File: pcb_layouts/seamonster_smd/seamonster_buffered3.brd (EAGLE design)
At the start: 172.5 x 106.5 mm, 132 parts, among them IC1 7808DT, IC2 4051D, IC3 4051D, IC4 DG408DY, IC5 4046D, IC6 40106D, IC7 4070D, IC8 4046D, IC9 4040D, Q1 THONKICONNNEW, Q2 THONKICONNNEW, Q3 THONKICONNNEW, Q4 THONKICONNNEW, Q5 THONKICONNNEW, Q6 THONKICONNNEW, SW1 SPDT ON-ON, SW2 SPDT ON-ON, SW3 SPDT ON-ON, SW4 SPDT ON-ON, U1 TL084, U2 TL084, U3 TL084

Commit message: finished routing, working on silkscreen
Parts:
- removed C30, C31, C32, C33, C34, C35: (no value), SparkFun-Capacitors:0805
- added C36, C37, C38, C39, C40, C41: (no value), SparkFun-Capacitors:CPOL-RADIAL-10UF-25V
- added CVCO1, CVCO2: 1µF, SparkFun-Capacitors:0805
- added U4: TL084D, linear:SO14
- C23, C24: value 1µF -> 0.1µF
- IC2: value 4051D -> 40106D; device 40xx:SO16 -> 40xx:SO14
- IC3: value 4051D -> 4040D
- IC4: value DG408DY -> 4051D; device maxim:SO16 -> 40xx:SO16
- IC5: value 4046D -> 4051D
- IC6: value 40106D -> DG408DY; device 40xx:SO14 -> maxim:SO16
- IC7: value 4070D -> 4046D; device 40xx:SO14 -> 40xx:SO16
- IC9: value 4040D -> 4070D; device 40xx:SO16 -> 40xx:SO14
- R1, R10, R11, R12, R13, R14, R2, R3, R4, R5, R6, R7, R8, R9: value (none) -> 270Ω
- moved IC3 126.9 mm to (133.3, 38.1), turned to 0 degrees
- moved IC9 118.1 mm to (21.3, 75.2), flipped to the bottom, turned to 180 degrees
- moved IC7 100.3 mm to (118.6, 51.0), flipped to the top, turned to 0 degrees
- moved IC4 89.2 mm to (19.7, 94.6), turned to 90 degrees
- moved IC5 74.8 mm to (57.8, 94.6), turned to 90 degrees
- moved IC6 66.3 mm to (105.4, 69.8), flipped to the top, turned to 270 degrees
- moved IC2 26.5 mm to (39.4, 75.6), flipped to the bottom, turned to 180 degrees
- moved C23 14.6 mm to (112.3, 32.5), turned to 270 degrees
- moved C24 6.80 mm to (111.3, 39.6), turned to 180 degrees
- moved C17 2.03 mm to (33.0, 75.1), flipped to the top
- moved C5 2.00 mm to (47.0, 56.0)
- moved U$2 1.14 mm to (161.5, 64.3)
- moved C1 1.02 mm to (108.2, 33.0)
- moved C20 0.71 mm to (14.8, 72.8)
- moved C27 0.51 mm to (125.6, 38.1)
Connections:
- removed net N$73: CCO1.P$3_SLEEVE, CCO2.P$3_SLEEVE, CCO3.P$3_SLEEVE, CCO4.P$3_SLEEVE, COMPLEX1.P$3_SLEEVE, COMPLEX2.P$3_SLEEVE
- removed net Q1: IC9.9, J1.2, Q1.P$1_TIP, R9.1
- new net N$61: IC3.9, U3.10
- new net Q1BUFFERED: J1.2, Q1.P$1_TIP, R9.1, U3.8, U3.9
- new net Q2BUFFERED: J2.2, Q2.P$1_TIP, R10.1, U3.13, U3.14
- new net Q3BUFFERED: J3.2, Q3.P$1_TIP, R11.1, U4.1, U4.2
- new net Q4BUFFERED: Q4.P$1_TIP, R12.1, U4.6, U4.7
- new net Q5BUFFERED: Q5.P$1_TIP, R13.1, U4.8, U4.9
- new net Q6BUFFERED: Q6.P$1_TIP, R14.1, U4.13, U4.14
- net A: now also IC4.11, IC5.11, IC6.1; no longer IC2.11, IC3.11, IC4.1
- net B: now also IC4.10, IC5.10, IC6.16; no longer IC2.10, IC3.10, IC4.16
- net C: now also IC4.9, IC5.9, IC6.15; no longer IC2.9, IC3.9, IC4.15
- net CCO1_BUFFERED: now also IC9.2; no longer IC7.2
- net CCO2_BUFFERED: now also IC9.6; no longer IC7.6
- net CCO3_BUFFERED: now also IC9.9; no longer IC7.9
- net CCO4_BUFFERED: now also IC9.13; no longer IC7.13
- net CV_OUT: now also IC4.3; no longer IC3.3
- net CV_OUT_BUFFERED: now also IC7.9; no longer IC5.9
- net GND: now also C23.2, C24.2, C36.2, C37.2, C38.2, C39.2, C40.2, C41.2, CCO1.P$3_SLEEVE, CCO2.P$3_SLEEVE, CCO3.P$3_SLEEVE, CCO4.P$3_SLEEVE, COMPLEX1.P$3_SLEEVE, COMPLEX2.P$3_SLEEVE, IC3.11, IC4.6, IC4.7, IC4.8, IC5.6, IC5.7, IC6.14, IC7.5, IC7.8, IC9.7; no longer C30.2, C31.2, C32.2, C33.2, C34.2, C35.2, IC2.6, IC2.8, IC3.6, IC3.7, IC4.14, IC5.5, IC6.7, IC7.7, IC9.11, IC9.8
- net INV_B_IN: now also IC2.3; no longer IC6.3
- net INV_B_OUT: now also IC2.4; no longer IC6.4
- net INV_C_IN: now also IC2.5; no longer IC6.5
- net INV_C_OUT: now also IC2.6; no longer IC6.6
- net INV_D_IN: now also IC2.9; no longer IC6.9
- net INV_D_OUT: now also IC2.8; no longer IC6.8
- net INV_E_IN: now also IC2.11; no longer IC6.11
- net INV_E_OUT: now also IC2.10; no longer IC6.10
- net MUX1: now also IC6.4; no longer IC4.4
- net MUX2: now also IC6.5; no longer IC4.5
- net MUX3: now also IC6.6; no longer IC4.6
- net MUX4: now also IC6.7; no longer IC4.7
- net MUX5: now also IC6.12; no longer IC4.12
- net MUX6: now also IC6.11; no longer IC4.11
- net MUX7: now also IC6.10; no longer IC4.10
- net MUX8: now also IC6.9; no longer IC4.9
- net N$1: now also IC6.8; no longer IC4.8
- net N$18: now also IC4.13; no longer IC3.13
- net N$19: now also IC5.13; no longer IC2.13
- net N$2: now also IC2.1; no longer IC6.1
- net N$20: now also IC5.14; no longer IC2.14
- net N$21: now also IC5.15; no longer IC2.15
- net N$22: now also IC5.12; no longer IC2.12
- net N$23: now also IC5.1; no longer IC2.1
- net N$24: now also IC5.5; no longer IC2.5
- net N$25: now also IC5.2; no longer IC2.2
- net N$26: now also IC5.4; no longer IC2.4
- net N$27: now also IC4.14; no longer IC3.14
- net N$28: now also IC4.15; no longer IC3.15
- net N$29: now also IC4.12; no longer IC3.12
- net N$3: now also C36.1; no longer C30.1
- net N$30: now also IC4.1; no longer IC3.1
- net N$31: now also IC4.5; no longer IC3.5
- net N$32: now also IC4.2; no longer IC3.2
- net N$33: now also IC4.4; no longer IC3.4
- net N$35: now also IC9.3, IC9.5; no longer IC7.3, IC7.5
- net N$36: now also IC9.10, IC9.12; no longer IC7.10, IC7.12
- net N$38: now also IC9.4; no longer IC7.4
- net N$39: now also IC9.11; no longer IC7.11
- net N$4: now also C37.1; no longer C31.1
- net N$40: now also IC7.12; no longer IC5.12
- net N$43: now also IC2.2; no longer IC6.2
- net N$44: now also CVCO1.1, IC7.6; no longer C23.1, IC5.6
- net N$45: now also CVCO1.2, IC7.7; no longer C23.2, IC5.7
- net N$48: now also CVCO2.1; no longer C24.1
- net N$49: now also CVCO2.2; no longer C24.2
- net N$5: now also C38.1; no longer C32.1
- net N$50: now also IC3.10; no longer IC9.10
- net N$6: now also C39.1; no longer C33.1
- net N$7: now also C40.1; no longer C34.1
- net N$75: now also IC7.11; no longer IC5.11
- net N$8: now also C41.1; no longer C35.1
- net Q2: now also IC3.7, U3.12; no longer IC9.7, J2.2, Q2.P$1_TIP, R10.1
- net Q3: now also IC3.6, U4.3; no longer IC9.6, J3.2, Q3.P$1_TIP, R11.1
- net Q4: now also IC3.5, U4.5; no longer IC9.5, Q4.P$1_TIP, R12.1
- net Q5: now also IC3.3, U4.10; no longer IC9.3, Q5.P$1_TIP, R13.1
- net Q6: now also IC3.2, U4.12; no longer IC9.2, Q6.P$1_TIP, R14.1
- net V+: now also C23.1, IC6.13, IC6.2, U4.4; no longer IC4.13, IC4.2
- net V-: now also C24.1, IC6.3, U4.11; no longer IC4.3
- net VCC: now also IC2.14, IC4.16, IC5.3, IC7.16, IC9.14; no longer IC2.16, IC2.3, IC6.14, IC7.14, IC9.16
- net VCO1_OUT: now also IC7.4; no longer IC5.4
- net VCO2_OUT_BUFFERED: now also IC9.1, IC9.8; no longer IC7.1, IC7.8
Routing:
- net Q1BUFFERED: track 0.00 -> 201.7 mm, vias 0 -> 3
- net Q2BUFFERED: track 0.00 -> 197.9 mm, vias 0 -> 3
- net N$61: track 0.00 -> 164.9 mm, vias 0 -> 4
- net N$39: track 0.00 -> 161.7 mm, vias 0 -> 2
- net VCO1_OUT: track 0.00 -> 126.9 mm
- net N$9: track 50.5 -> 171.8 mm, vias 0 -> 3
- net Q2: track 60.7 -> 173.3 mm, vias 1 -> 4
- net VCO2_OUT_BUFFERED: track 1.27 -> 105.8 mm, vias 0 -> 5
- net N$38: track 0.00 -> 81.6 mm, vias 0 -> 2
- net Q1: track 77.3 -> 0.00 mm, vias 1 -> 0
- net VCO2_OUT: track 0.00 -> 76.6 mm, vias 0 -> 2
- net Q3BUFFERED: track 0.00 -> 71.7 mm, vias 0 -> 1
- net V-: track 158.0 -> 223.7 mm, vias 1 -> 3
- net N$6: track 5.22 -> 68.2 mm
- net CV_OUT_BUFFERED: track 110.9 -> 173.6 mm, vias 0 -> 1
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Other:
- board size 172.5 x 106.5 mm -> 172.5 x 106.7 mm
- board text added: "SeaMonster"
- board text added: "clock oscillator timing capacitors"
- board text added: "fixed frequency oscillator timing capacitors"
- board text added: "revision 1.0 designed by Shaurjya Banerjee september 2018 wholesomecircuits.com"
- board text added: "solder jumpers closed to normal the clock outputs to multiplexer inputs"
- board text added: "voltage controlled oscillator timing capacitors"

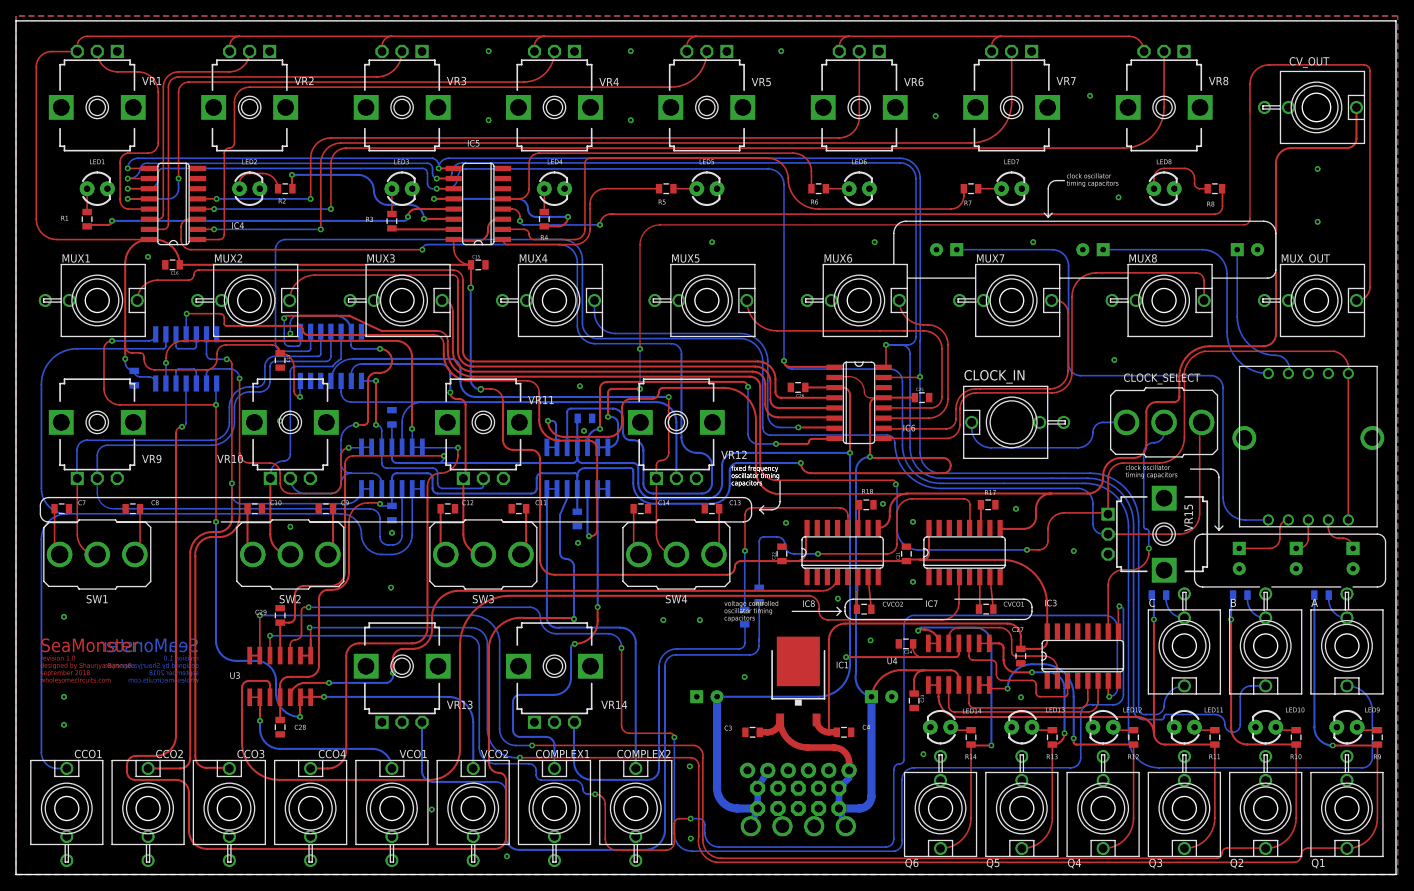
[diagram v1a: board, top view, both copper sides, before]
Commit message: worked on ai panel mockup, added TH capacitor optionally
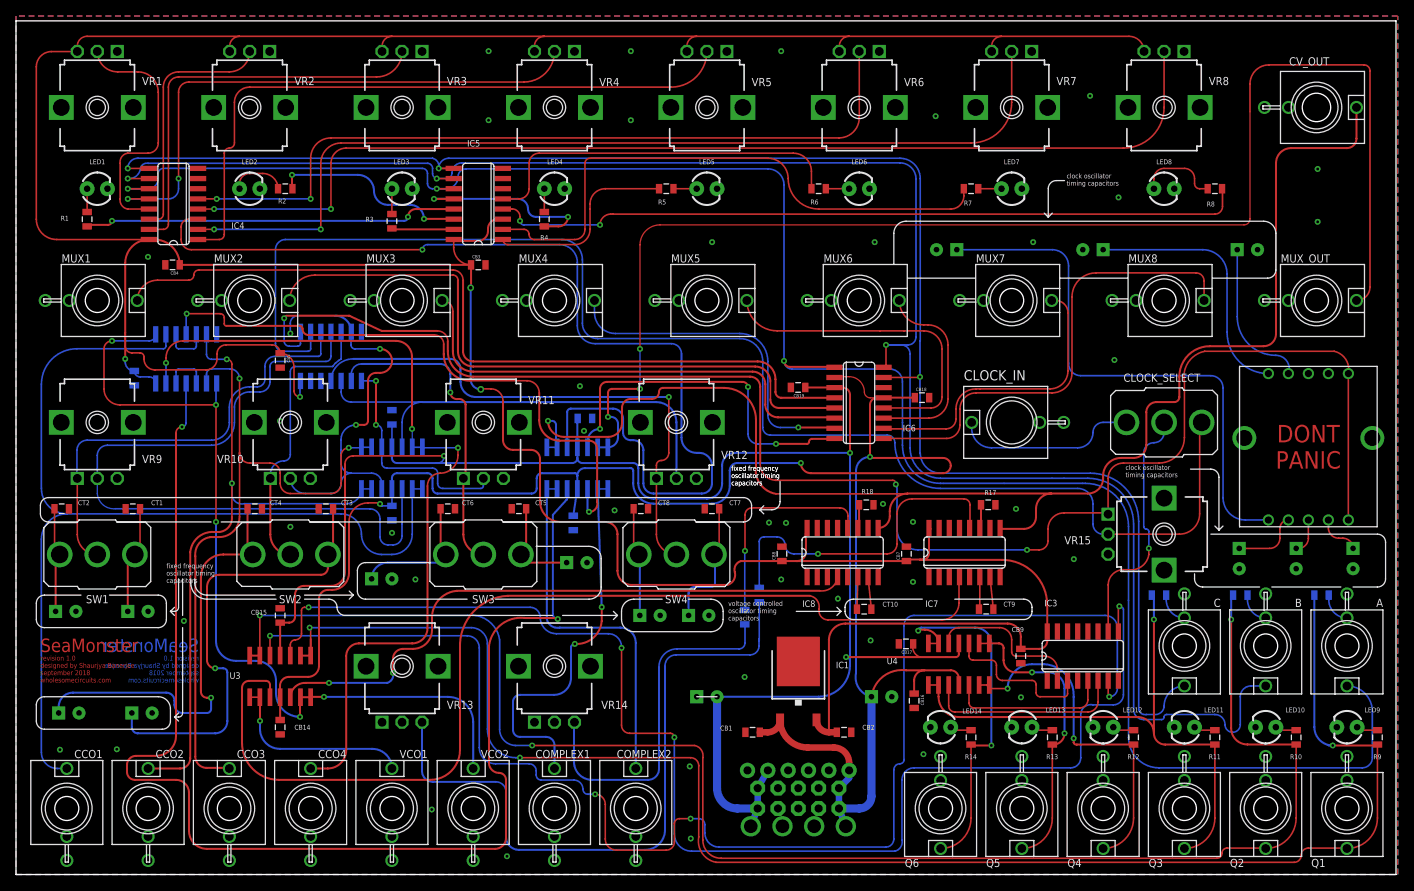
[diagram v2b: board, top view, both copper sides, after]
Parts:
- removed C18: 0.1µF, SparkFun-Capacitors:0805
- added CB12: 0.1µF, SparkFun-Capacitors:0805
- added CTH1, CTH2, CTH3, CTH4, CTH5, CTH6, CTH7, CTH8: (no value), SparkFun-Capacitors:CPOL-RADIAL-10UF-25V
- CT1, CT3, CT5, CT7: value 1µF -> (none)
- CT2, CT4, CT6, CT8: value 0.1µF -> (none)
- U$2: value ALPHA_ROTARY_SWITCH -> CLOCK RATE SELECT
- renumbered C10 to CT4, C11 to CT5, C12 to CT6, C13 to CT7, C14 to CT8, C15 to CB3, C16 to CB4, C17 to CB5, C19 to CB13, C20 to CB6, C21 to CB7, C22 to CB8, C23 to CB16, C24 to CB17, C25 to CB18, C26 to CB19, C27 to CB9, C28 to CB14, C29 to CB15, C3 to CB1, C36 to CCLK1, C37 to CCLK2, C38 to CCLK3, C39 to CCLK4, C4 to CB2, C40 to CCLK5, C41 to CCLK6, C5 to CB10, C6 to CB11, C7 to CT2, C8 to CT1, C9 to CT3, CVCO1 to CT9, CVCO2 to CT10
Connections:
- net GND: now also CB12.2, CTH1.2, CTH2.2, CTH3.2, CTH4.2, CTH5.2, CTH6.2, CTH7.2, CTH8.2; no longer C18.2
- net N$47: now also CTH2.1
- net N$52: now also CTH1.1
- net N$55: now also CTH4.1
- net N$56: now also CTH3.1
- net N$59: now also CTH6.1
- net N$60: now also CTH5.1
- net N$63: now also CTH8.1
- net N$64: now also CTH7.1
- net V+: now also CB12.1; no longer C18.1
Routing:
- net N$56: track 5.98 -> 56.8 mm, vias 0 -> 1
- net N$55: track 5.98 -> 53.1 mm, vias 0 -> 1
- net N$59: track 5.98 -> 16.5 mm
- net N$64: track 5.98 -> 16.2 mm
- net N$63: track 5.98 -> 13.7 mm
- net N$52: track 5.98 -> 13.5 mm
- net N$47: track 5.98 -> 13.3 mm
- net N$38: track 81.6 -> 75.4 mm
- net N$60: track 5.98 -> 12.1 mm
- net N$39: track 161.7 -> 159.7 mm
- net V+: track 242.9 -> 243.4 mm
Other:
- board text added: "DONT PANIC"

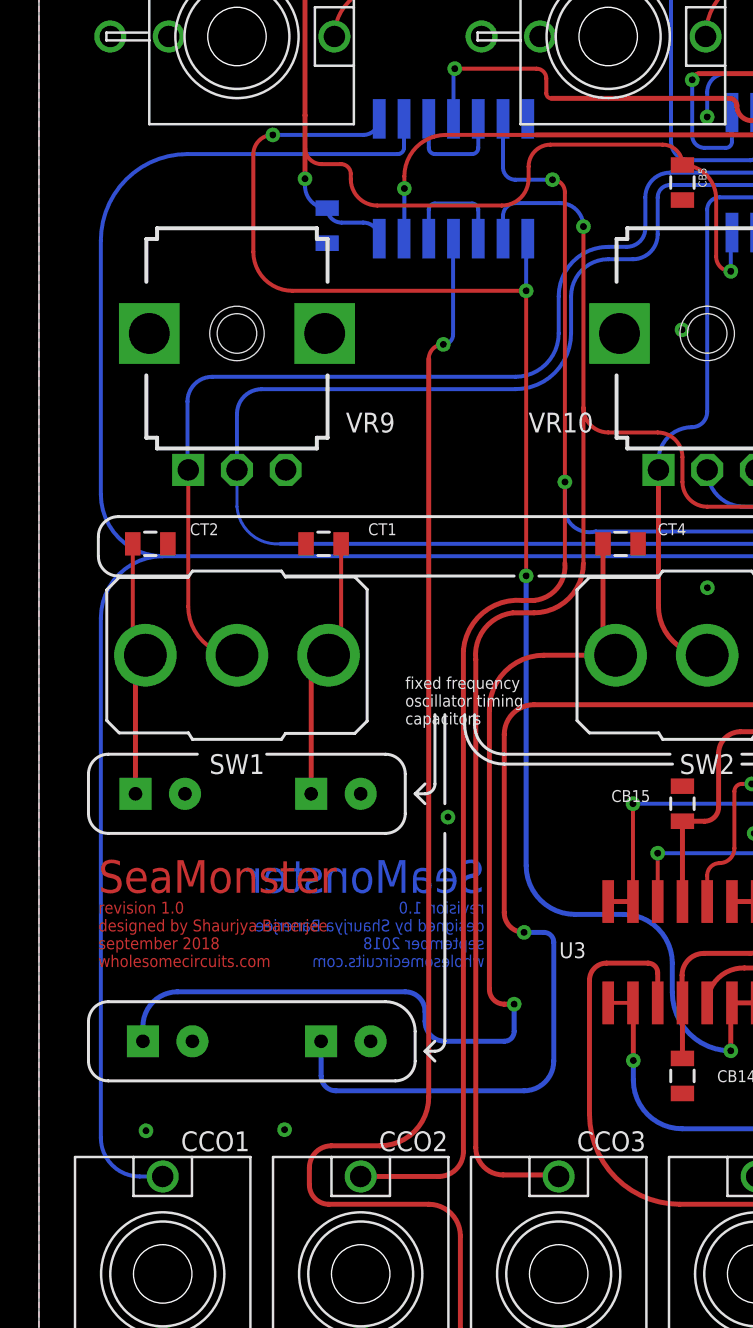
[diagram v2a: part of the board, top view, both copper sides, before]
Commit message: smd mk1 routing complete
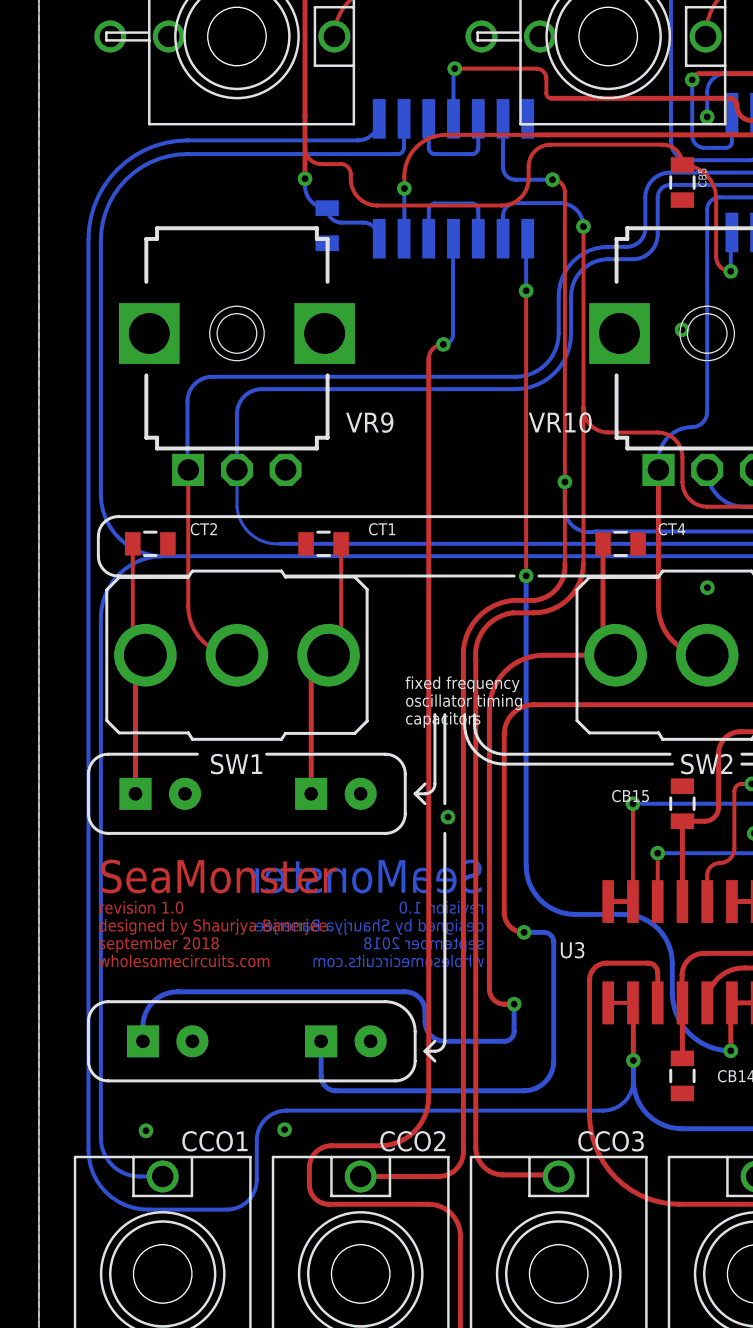
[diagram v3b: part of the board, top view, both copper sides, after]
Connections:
- net VCO1_OUT_BUFFERED: now also IC9.1
- net VCO2_OUT_BUFFERED: no longer IC9.1
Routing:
- net VCO1_OUT_BUFFERED: track 23.8 -> 121.6 mm
- net VCO2_OUT_BUFFERED: track 105.8 -> 78.7 mm, vias 5 -> 4
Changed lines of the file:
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@@
 <drawing>
 <settings>
-<setting alwaysvectorfont="yes"/>
+<setting alwaysvectorfont="no"/>
 <setting keepoldvectorfont="yes"/>
 <setting verticaltext="up"/>
@@
 <wire x1="30.5" y1="32.94" x2="30.5" y2="30" width="0.254" layer="1"/>
 <via x="30.5" y="30" extent="1-16" drill="0.35"/>
-<wire x1="30.5" y1="30" x2="30.5" y2="29" width="0.254" layer="16"/>
+<wire x1="30.5" y1="30" x2="30.5" y2="29.464" width="0.254" layer="16"/>
+<wire x1="30.5" y1="29.464" x2="30.5" y2="29" width="0.254" layer="16"/>
 <wire x1="30.5" y1="29" x2="33" y2="26.5" width="0.254" layer="16" curve="90"/>
 <wire x1="33" y1="26.5" x2="44.54" y2="26.5" width="0.254" layer="16"/>
 <wire x1="44.54" y1="26.5" x2="46.99" y2="24.05" width="0.254" layer="16" curve="-90"/>
+<contactref element="IC9" pad="1"/>
+<wire x1="17.4625" y1="78.3209" x2="16.3576" y2="77.216" width="0.2032" layer="16" curve="-90"/>
+<wire x1="7.62" y1="77.216" x2="2.54" y2="72.136" width="0.2032" layer="16" curve="90"/>
+<wire x1="2.54" y1="25.4" x2="5.588" y2="22.352" width="0.2032" layer="16" curve="90"/>
+<wire x1="11.176" y1="25.908" x2="12.7" y2="27.432" width="0.2032" layer="16" curve="-90"/>
+<wire x1="28.956" y1="27.432" x2="30.5" y2="28.976" width="0.2032" layer="16" curve="90"/>
+<wire x1="30.5" y1="28.976" x2="30.5" y2="29.464" width="0.2032" layer="16"/>
+<wire x1="16.3576" y1="77.216" x2="7.62" y2="77.216" width="0.2032" layer="16"/>
+<wire x1="2.54" y1="72.136" x2="2.54" y2="25.4" width="0.2032" layer="16"/>
+<wire x1="11.176" y1="23.876" x2="11.176" y2="25.908" width="0.2032" layer="16"/>
+<wire x1="12.7" y1="27.432" x2="28.956" y2="27.432" width="0.2032" layer="16"/>
+<wire x1="5.588" y1="22.352" x2="9.652" y2="22.352" width="0.2032" layer="16"/>
+<wire x1="9.652" y1="22.352" x2="11.176" y2="23.876" width="0.2032" layer="16" curve="90"/>
 </signal>
 <signal name="VCO2_OUT">
@@
 <wire x1="35.56" y1="32.96" x2="36.83" y2="32.96" width="0.254" layer="1"/>
 <contactref element="IC9" pad="8"/>
-<contactref element="IC9" pad="1"/>
 <wire x1="36.83" y1="32.96" x2="36.87" y2="33" width="0.2032" layer="1" curve="-90"/>
 <via x="38.5" y="33" extent="1-16" drill="0.35"/>
@@
 <via x="25" y="54.8728" extent="1-16" drill="0.35"/>
 <wire x1="25" y1="40" x2="25" y2="54.8728" width="0.254" layer="16"/>
-<wire x1="17.4625" y1="78.3209" x2="16.6416" y2="77.5" width="0.2032" layer="16" curve="-90"/>
-<wire x1="16.6416" y1="77.5" x2="12" y2="77.5" width="0.2032" layer="16"/>
-<via x="12" y="77.5" extent="1-16" drill="0.35"/>
-<wire x1="12" y1="77.5" x2="11" y2="76.5" width="0.2032" layer="1" curve="90"/>
-<wire x1="11" y1="76.5" x2="11" y2="71.5" width="0.2032" layer="1"/>
-<wire x1="11" y1="71.5" x2="13" y2="69.5" width="0.2032" layer="1" curve="90"/>
-<wire x1="13" y1="69.5" x2="25" y2="69.5" width="0.2032" layer="1"/>
 </signal>
 <signal name="N$44">
